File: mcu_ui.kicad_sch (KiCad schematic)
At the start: 31 parts, among them J5 UPDI, SW1 EC11E18244A5, SW2 BAND, SW3 STEP, SW4 MENU, U4 ATtiny3226-SU

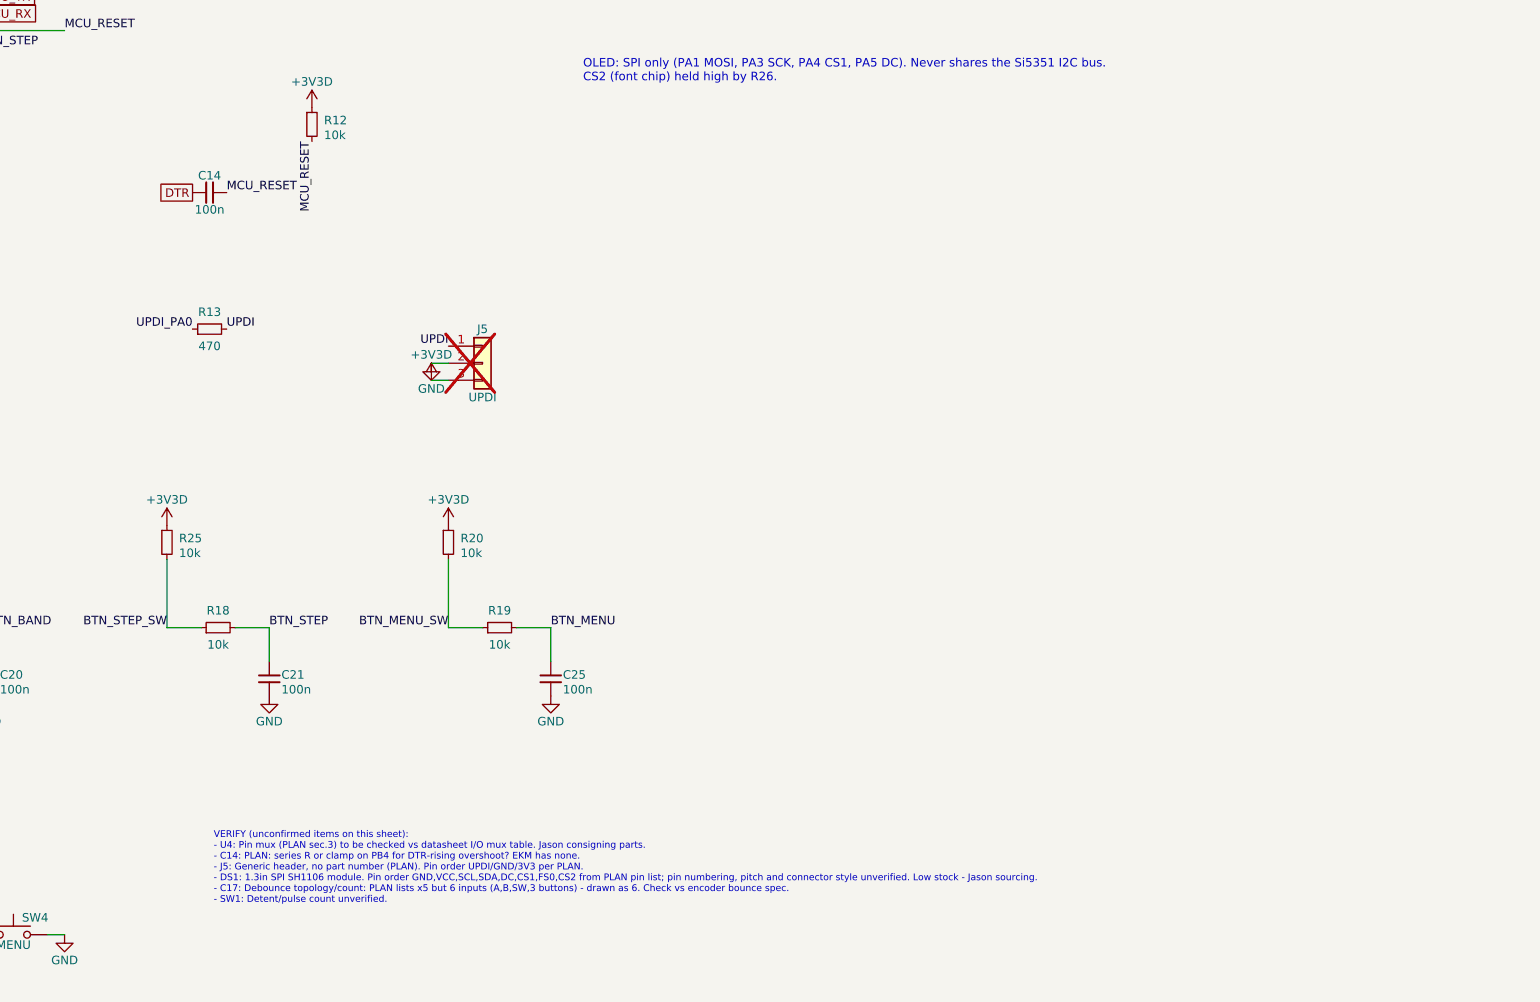
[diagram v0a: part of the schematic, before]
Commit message: UPDI: replicate EtherKeyerMini UPDI circuit (J5/R13/D4/D5/JP1/JP2); remove CP2102N LEDs D2/D3 + R10/R11, NC pins 13/14
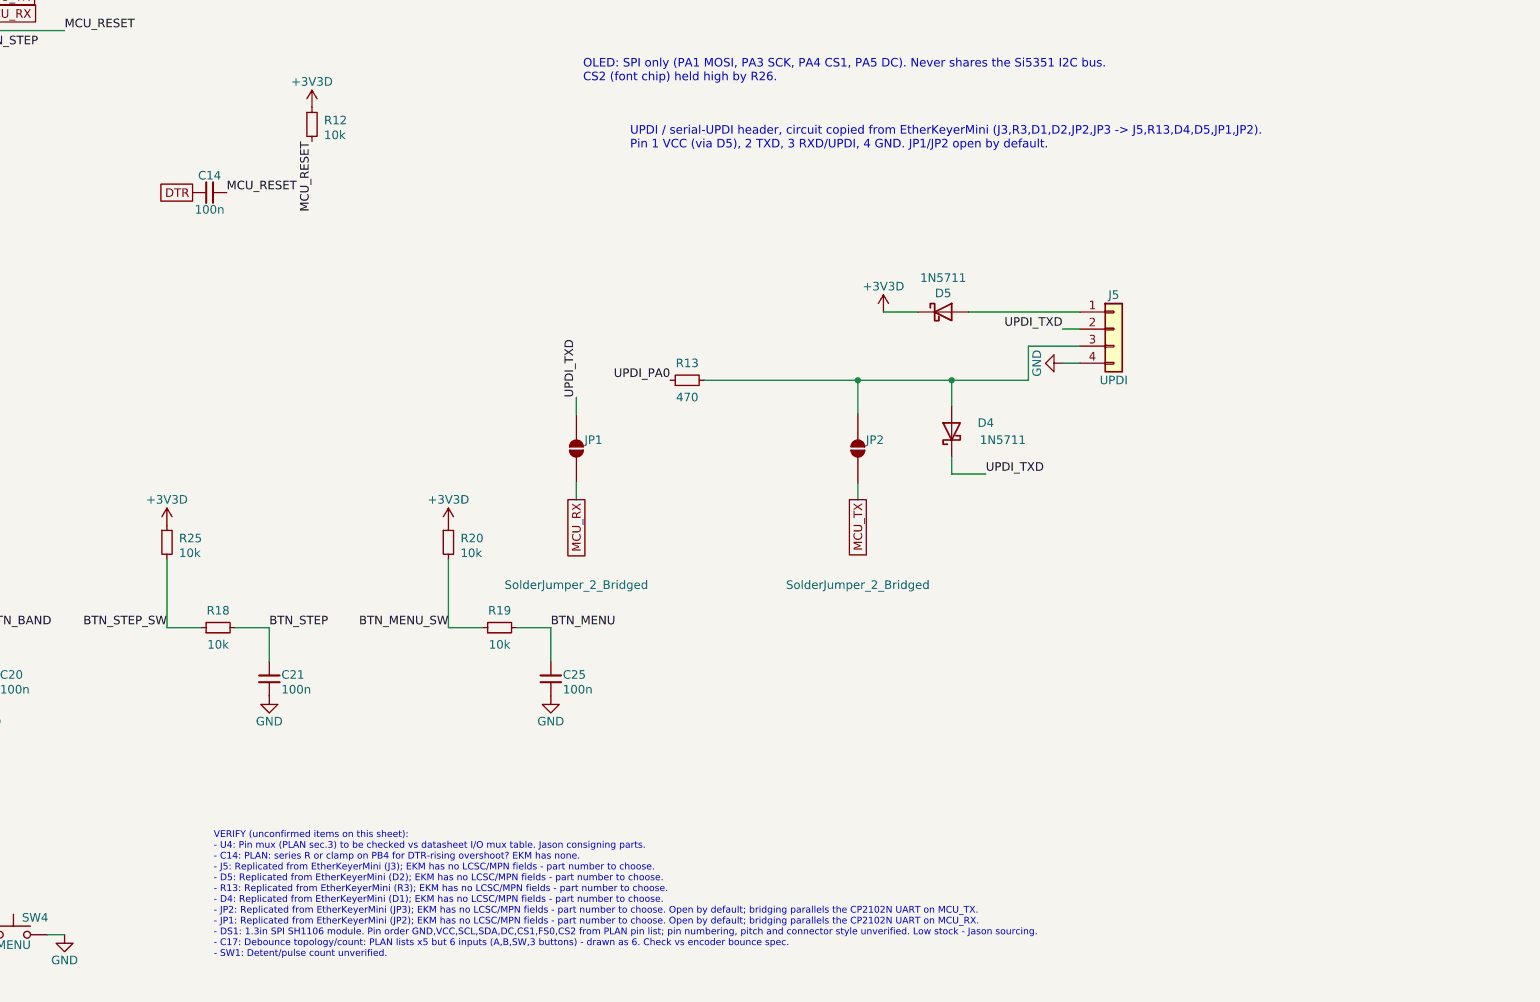
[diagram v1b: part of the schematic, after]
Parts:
- removed J5: UPDI, Connector_PinHeader_2.54mm:PinHeader_1x03_P2.54mm_Vertical, symbol Connector_Generic:Conn_01x03
- added D4, D5: 1N5711, Diode_THT:D_DO-35_SOD27_P7.62mm_Horizontal, symbol Device:D_Schottky
- added J5: UPDI, Connector_PinSocket_2.54mm:PinSocket_1x04_P2.54mm_Vertical, symbol Connector_Generic:Conn_01x04
- added JP1, JP2: SolderJumper_2_Bridged, Jumper:SolderJumper-2_P1.3mm_Open_RoundedPad1.0x1.5mm, symbol Jumper:SolderJumper_2_Open
- R13: footprint Resistor_SMD:R_0603_1608Metric -> Resistor_THT:R_Axial_DIN0207_L6.3mm_D2.5mm_P2.54mm_Vertical; LCSC C114669 -> (none); MPN RC0603FR-07470RL -> (none); Manufacturer YAGEO -> (none); VERIFY (none) -> Replicated from EtherKeyerMini (R3); EKM has no LCSC/MPN fi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
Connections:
- net +3V3D: now also D5.1 (K)
- net GND: now also J5.4 (Pin_4)
- net MCU_RX: now also JP1.1 (A)
- net MCU_TX: now also JP2.1 (A)
- net UPDI: no longer names the net of R13.2
- net UPDI: now also D4.2 (A), J5.3 (Pin_3), JP2.2 (B)
- new net: D5.2 (A), J5.1 (Pin_1)
- new net UPDI_TXD: D4.1 (K), J5.2 (Pin_2), JP1.2 (B)
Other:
- note added: "UPDI / serial-UPDI header, circuit copied from EtherKeyerMini (J3,R3,D1,D2,JP2,JP3 -> J5,R13,D4,D5,JP1,JP2). Pin 1 VCC (via D5), 2 TXD, 3 RXD/UPDI, 4 GND. JP1/JP2 open by default."
- note added: "VERIFY (unconfirmed items on this sheet): - U4: Pin mux (PLAN sec.3) to be checked vs datasheet I/O mux table. Jason consigning parts. - C14: PLAN: series R or clamp on PB4 for DTR-rising overshoot? EKM has none. - J5: Replicated from EtherKeyerMini (J3); EKM has no LCSC/MPN fields - part number to choose. - D5: Replicated from EtherKeyerMini (D2); EKM has no LCSC/MPN fields - part number to choo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"
- note removed: "VERIFY (unconfirmed items on this sheet): - U4: Pin mux (PLAN sec.3) to be checked vs datasheet I/O mux table. Jason consigning parts. - C14: PLAN: series R or clamp on PB4 for DTR-rising overshoot? EKM has none. - J5: Generic header, no part number (PLAN). Pin order UPDI/GND/3V3 per PLAN. - DS1: 1.3in SPI SH1106 module. Pin order GND,VCC,SCL,SDA,DC,CS1,FS0,CS2 from PLAN pin list; pin numbering, 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"

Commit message: Wire local connections (labels only for long/cross-sheet runs); +3V3_MCU diode-OR rail (D6/D5); drop UPDI JP1/JP2; fix C14 fields
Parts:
- removed JP1, JP2: SolderJumper_2_Bridged, Jumper:SolderJumper-2_P1.3mm_Open_RoundedPad1.0x1.5mm, symbol Jumper:SolderJumper_2_Open
- added D6: 1N5711, Diode_THT:D_DO-35_SOD27_P7.62mm_Horizontal, symbol Device:D_Schottky
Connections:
- net +3V3D: now also D6.2 (A); no longer C15.1, C16.1, D5.1 (K), R12.1, R20.1, R21.1, R22.1, R23.1, R24.1, R25.1, R26.1, U4.1 (VCC)
- net MCU_RESET: no longer names the net of C14.2, R12.2, U4.7 (PB4)
- new net +3V3_MCU: C15.1, C16.1, D5.1 (K), D6.1 (K), R12.1, R20.1, R21.1, R22.1, R23.1, R24.1, R25.1, R26.1, U4.1 (VCC)
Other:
- note added: "+3V3_MCU = +3V3D via D6 OR UPDI pin 1 via D5 (ATtiny only)."
- note added: "UPDI / serial-UPDI header, circuit copied from EtherKeyerMini (J3,R3,D1,D2 -> J5,R13,D4,D5; EKM JP2/JP3 omitted per Jason). Pin 1 VCC (via D5, feeds +3V3_MCU only), 2 TXD, 3 RXD/UPDI, 4 GND."
- note added: "VERIFY (unconfirmed items on this sheet): - U4: Pin mux (PLAN sec.3) to be checked vs datasheet I/O mux table. Jason consigning parts. - D6: ATtiny-only rail +3V3_MCU: diode-OR of +3V3D (D6) and UPDI header VCC (D5) so a programmer cannot back-feed +3V3D. Same 1N5711 as EKM D5 (no LCSC/MPN). MCU VDD ~2.9-3.0 V (0.3-0.4 V drop): check ATtiny VIH/VIL vs CP2102N TXD (3.3 V VIO, exceeds MCU VDD by ~0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"
- note removed: "UPDI / serial-UPDI header, circuit copied from EtherKeyerMini (J3,R3,D1,D2,JP2,JP3 -> J5,R13,D4,D5,JP1,JP2). Pin 1 VCC (via D5), 2 TXD, 3 RXD/UPDI, 4 GND. JP1/JP2 open by default."
- note removed: "VERIFY (unconfirmed items on this sheet): - U4: Pin mux (PLAN sec.3) to be checked vs datasheet I/O mux table. Jason consigning parts. - C14: PLAN: series R or clamp on PB4 for DTR-rising overshoot? EKM has none. - J5: Replicated from EtherKeyerMini (J3); EKM has no LCSC/MPN fields - part number to choose. - D5: Replicated from EtherKeyerMini (D2); EKM has no LCSC/MPN fields - part number to choo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"

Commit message: Drop +3V3_MCU/D5/D6: U4 and pull-ups back on +3V3D; J5 pin 1 = +3V3D VCC reference (USB-powered programming)
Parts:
- removed D5, D6: 1N5711, Diode_THT:D_DO-35_SOD27_P7.62mm_Horizontal, symbol Device:D_Schottky
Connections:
- net +3V3_MCU is gone; now on net +3V3D: C15.1, C16.1, R12.1, R20.1, R21.1, R22.1, R23.1, R24.1, R25.1, R26.1, U4.1 (VCC)
- net +3V3D: now also J5.1 (Pin_1)
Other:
- note added: "Pin 1 = VCC reference for programmer; board must be USB-powered while programming."
- note added: "UPDI / serial-UPDI header, circuit copied from EtherKeyerMini (J3,R3,D1 -> J5,R13,D4; EKM D2/JP2/JP3 omitted per Jason). Pin 1 VCC ref (+3V3D), 2 TXD, 3 RXD/UPDI, 4 GND."
- note added: "VERIFY (unconfirmed items on this sheet): - U4: Pin mux (PLAN sec.3) to be checked vs datasheet I/O mux table. Jason consigning parts. - C14: PLAN: series R or clamp on PB4 for DTR-rising overshoot? EKM has none. - J5: Replicated from EtherKeyerMini (J3); EKM has no LCSC/MPN fields - part number to choose. - R13: Replicated from EtherKeyerMini (R3); EKM has no LCSC/MPN fields - part number to cho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"
- note removed: "+3V3_MCU = +3V3D via D6 OR UPDI pin 1 via D5 (ATtiny only)."
- note removed: "UPDI / serial-UPDI header, circuit copied from EtherKeyerMini (J3,R3,D1,D2 -> J5,R13,D4,D5; EKM JP2/JP3 omitted per Jason). Pin 1 VCC (via D5, feeds +3V3_MCU only), 2 TXD, 3 RXD/UPDI, 4 GND."
- note removed: "VERIFY (unconfirmed items on this sheet): - U4: Pin mux (PLAN sec.3) to be checked vs datasheet I/O mux table. Jason consigning parts. - D6: ATtiny-only rail +3V3_MCU: diode-OR of +3V3D (D6) and UPDI header VCC (D5) so a programmer cannot back-feed +3V3D. Same 1N5711 as EKM D5 (no LCSC/MPN). MCU VDD ~2.9-3.0 V (0.3-0.4 V drop): check ATtiny VIH/VIL vs CP2102N TXD (3.3 V VIO, exceeds MCU VDD by ~0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"
